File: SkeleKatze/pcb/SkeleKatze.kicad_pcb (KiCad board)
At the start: 2 copper layers, 54.5 x 82.9 mm, 6 parts, among them SW2 SW_Push

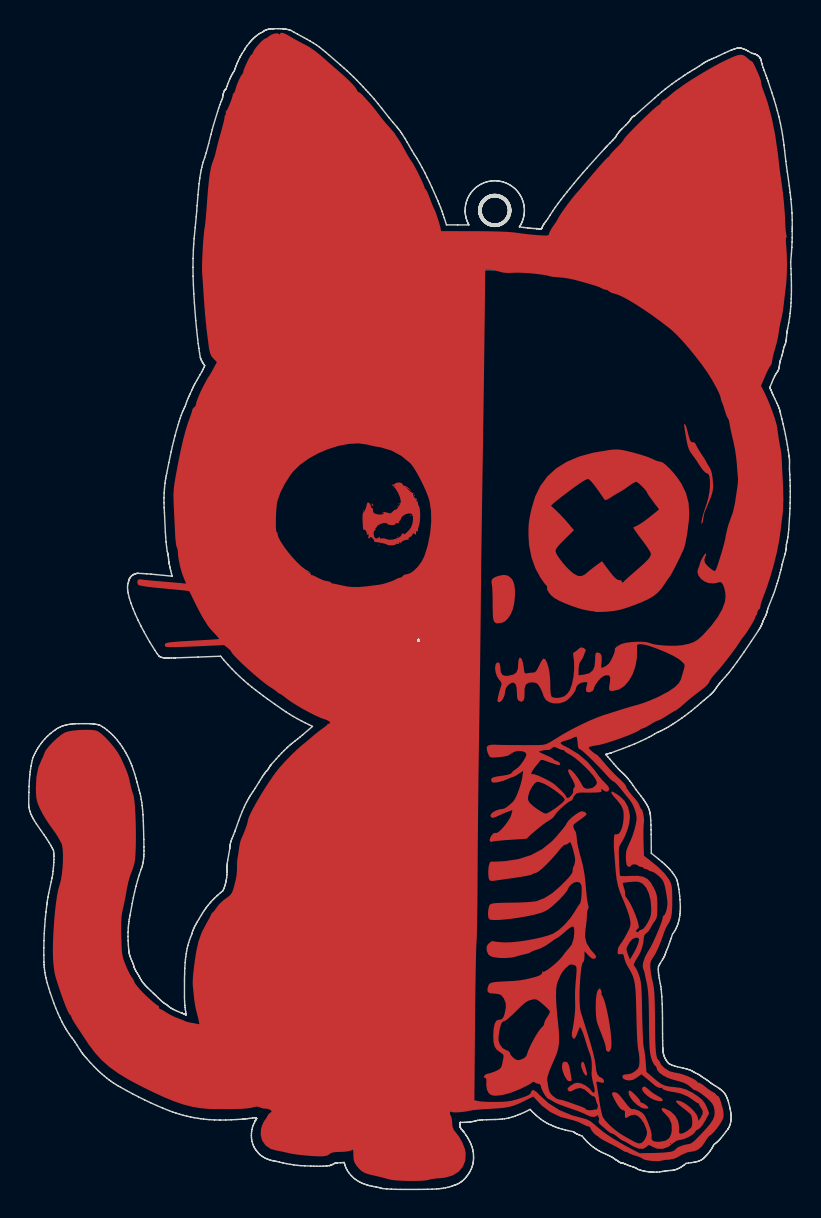
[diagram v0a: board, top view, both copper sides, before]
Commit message: Adds an explicit drill hole rather than relying on an edgecut
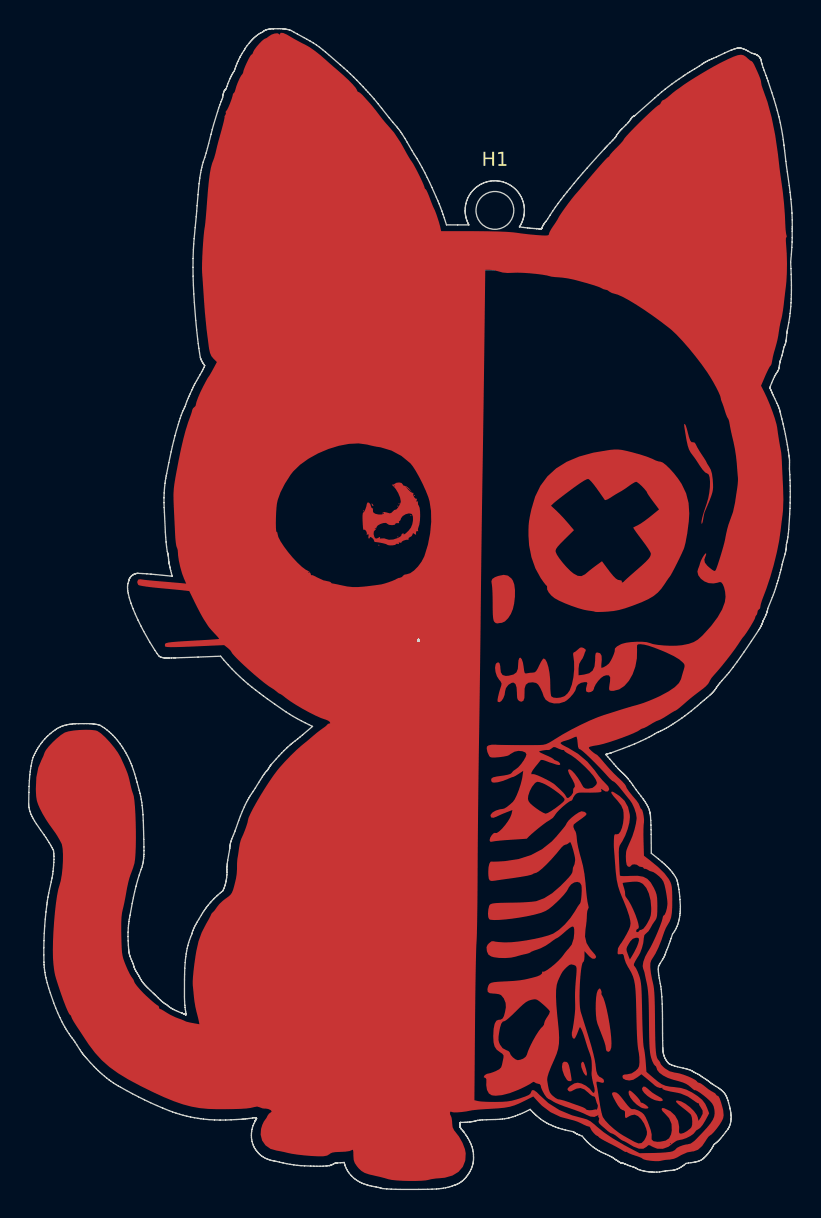
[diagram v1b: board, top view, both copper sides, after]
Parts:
- added H1: MountingHole, MountingHole:MountingHole_2.7mm_M2.5, F.Cu at (221.0, 48.9)
- moved D1 7.18 mm to (203.0, 61.5), turned to -45 degrees
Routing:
- net GND: track 81.6 -> 85.0 mm
- net Net-(D1-A): track 64.0 -> 66.3 mm
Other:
- outline, holes or cut-outs redrawn
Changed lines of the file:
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@@
 		(embedded_fonts no)
 	)
+	(footprint "MountingHole:MountingHole_2.7mm_M2.5"
+		(layer "F.Cu")
+		(at 220.955876 48.864324)
+		(descr "Mounting Hole 2.7mm, M2.5, no annular, generated by kicad-footprint-generator mountinghole.py")
+		(tags "mountinghole M2.5")
+		(property "Reference" "H1"
+			(at 0 -3.65 0)
+			(layer "F.SilkS")
+			(effects
+				(font
+					(size 1 1)
+					(thickness 0.15)
+				)
+			)
+		)
+		(property "Value" "MountingHole"
+			(at 0 3.65 0)
+			(layer "F.Fab")
+			(effects
+				(font
+					(size 1 1)
+					(thickness 0.15)
+				)
+			)
+		)
+		(property "Datasheet" ""
+			(at 0 0 0)
+			(layer "F.Fab")
+			(hide yes)
+			(effects
+				(font
+					(size 1.27 1.27)
+				)
+			)
+		)
+		(property "Description" "Mounting Hole without connection"
+			(at 0 0 0)
+			(layer "F.Fab")
+			(hide yes)
+			(effects
+				(font
+					(size 1.27 1.27)
+				)
+			)
+		)
+		(property ki_fp_filters "MountingHole*")
+		(sheetname "/")
+		(sheetfile "SkeleKatze.kicad_sch")
+		(units
+			(unit
+				(name "A")
+				(pins)
+			)
+		)
+		(duplicate_pad_numbers_are_jumpers no)
+		(fp_circle
+			(center 0 0)
+			(end 2.7 0)
+			(stroke
+				(width 0.15)
+				(type solid)
+			)
+			(fill no)
+			(layer "Cmts.User")
+		)
+		(fp_circle
+			(center 0 0)
+			(end 2.95 0)
+			(stroke
+				(width 0.05)
+				(type solid)
+			)
+			(fill no)
+			(layer "F.CrtYd")
+		)
+		(fp_text user "${REFERENCE}"
+			(at 0 0 0)
+			(layer "F.Fab")
+			(effects
+				(font
+					(size 1 1)
+					(thickness 0.15)
+				)
+			)
+		)
+		(pad "" np_thru_hole circle
+			(at 0 0)
+			(size 2.7 2.7)
+			(drill 2.7)
+			(layers "*.Cu" "*.Mask")
+		)
+		(embedded_fonts no)
+	)
 	(footprint "ZAM-Parts:LED D5.0mm SMD"
 		(layer "B.Cu")
-		(at 209.83 59.300002 -90)
+		(at 203 61.5 -45)
 		(property "Reference" "D1"
-			(at 4.572 -1.27 90)
+			(at 4.572 -1.27 135)
 			(unlocked yes)
 			(layer "B.SilkS")
@@
 		)
 		(property "Value" "LED"
-			(at 0 -4.572 90)
+			(at 0 -4.572 135)
 			(unlocked yes)
 			(layer "B.Fab")
@@
 		)
 		(property "Datasheet" ""
-			(at 0 0 90)
+			(at 0 0 135)
 			(unlocked yes)
 			(layer "B.Fab")
@@
 		)
 		(property "Description" "Light emitting diode"
-			(at 0 0 90)
+			(at 0 0 135)
 			(unlocked yes)
 			(layer "B.Fab")
@@
 		)
 		(property "Sim.Pins" "1=K 2=A"
-			(at 0 0 270)
+			(at 0 0 315)
 			(unlocked yes)
 			(layer "B.Fab")
@@
 		(duplicate_pad_numbers_are_jumpers no)
 		(fp_text user "+"
-			(at -1.016 -5.08 90)
+			(at -1.016 -5.08 135)
 			(unlocked yes)
 			(layer "B.SilkS")
@@
 		)
 		(pad "1" smd roundrect
-			(at 0 0 270)
+			(at 0 0 315)
 			(size 4 1.5)
 			(layers "B.Cu" "B.Mask" "B.Paste")
@@
 		)
 		(pad "2" smd roundrect
-			(at 0 -2.54 270)
+			(at 0 -2.54 315)
 			(size 4 1.5)
 			(layers "B.Cu" "B.Mask" "B.Paste")
@@
 	(gr_poly
 		(pts
-			(xy 221.00091 47.807604) (xy 221.054657 47.811691) (xy 221.107623 47.818422) (xy 221.15974 47.827729)
-			(xy 221.210943 47.839546) (xy 221.261165 47.853808) (xy 221.31034 47.870447) (xy 221.358401 47.889396)
-			(xy 221.405281 47.91059) (xy 221.450914 47.933962) (xy 221.495234 47.959446) (xy 221.538174 47.986974)
-			(xy 221.579667 48.016481) (xy 221.619648 48.047899) (xy 221.658049 48.081163) (xy 221.694804 48.116206)
-			(xy 221.729847 48.152961) (xy 221.763111 48.191362) (xy 221.79453 48.231343) (xy 221.824036 48.272836)
-			(xy 221.851565 48.315776) (xy 221.877048 48.360096) (xy 221.90042 48.405729) (xy 221.921614 48.45261)
-			(xy 221.940564 48.50067) (xy 221.957202 48.549845) (xy 221.971464 48.600067) (xy 221.983281 48.65127)
-			(xy 221.992589 48.703387) (xy 221.999319 48.756352) (xy 222.003406 48.810099) (xy 222.004783 48.864561)
-			(xy 222.003406 48.919022) (xy 221.999319 48.972769) (xy 221.992589 49.025734) (xy 221.983281 49.077851)
-			(xy 221.971464 49.129054) (xy 221.957202 49.179276) (xy 221.940564 49.228451) (xy 221.921614 49.276511)
-			(xy 221.90042 49.323391) (xy 221.877048 49.369025) (xy 221.851565 49.413345) (xy 221.824036 49.456284)
-			(xy 221.79453 49.497778) (xy 221.763111 49.537759) (xy 221.729847 49.57616) (xy 221.694804 49.612915)
-			(xy 221.658049 49.647958) (xy 221.619648 49.681222) (xy 221.579667 49.71264) (xy 221.538174 49.742147)
-			(xy 221.495234 49.769675) (xy 221.450914 49.795159) (xy 221.405281 49.818531) (xy 221.358401 49.839725)
-			(xy 221.31034 49.858675) (xy 221.261165 49.875313) (xy 221.210943 49.889575) (xy 221.15974 49.901392)
-			(xy 221.107623 49.9107) (xy 221.054657 49.91743) (xy 221.00091 49.921517) (xy 220.946449 49.922894)
-			(xy 220.891987 49.921517) (xy 220.83824 49.91743) (xy 220.785274 49.9107) (xy 220.733157 49.901392)
-			(xy 220.681954 49.889575) (xy 220.631732 49.875313) (xy 220.582557 49.858675) (xy 220.534496 49.839725)
-			(xy 220.487616 49.818531) (xy 220.441983 49.795159) (xy 220.397663 49.769675) (xy 220.354723 49.742147)
-			(xy 220.31323 49.71264) (xy 220.273249 49.681222) (xy 220.234848 49.647958) (xy 220.198093 49.612915)
-			(xy 220.16305 49.57616) (xy 220.129786 49.537759) (xy 220.098367 49.497778) (xy 220.068861 49.456284)
-			(xy 220.041332 49.413345) (xy 220.015849 49.369025) (xy 219.992477 49.323391) (xy 219.971283 49.276511)
-			(xy 219.952333 49.228451) (xy 219.935695 49.179276) (xy 219.921433 49.129054) (xy 219.909616 49.077851)
-			(xy 219.900309 49.025734) (xy 219.893578 48.972769) (xy 219.889491 48.919022) (xy 219.888114 48.864561)
-			(xy 219.889491 48.810099) (xy 219.893578 48.756352) (xy 219.900309 48.703387) (xy 219.909616 48.65127)
-			(xy 219.921433 48.600067) (xy 219.935695 48.549845) (xy 219.952333 48.50067) (xy 219.971283 48.45261)
-			(xy 219.992477 48.405729) (xy 220.015849 48.360096) (xy 220.041332 48.315776) (xy 220.068861 48.272836)
-			(xy 220.098367 48.231343) (xy 220.129786 48.191362) (xy 220.16305 48.152961) (xy 220.198093 48.116206)
-			(xy 220.234848 48.081163) (xy 220.273249 48.047899) (xy 220.31323 48.016481) (xy 220.354723 47.986974)
-			(xy 220.397663 47.959446) (xy 220.441983 47.933962) (xy 220.487616 47.91059) (xy 220.534496 47.889396)
-			(xy 220.582557 47.870447) (xy 220.631732 47.853808) (xy 220.681954 47.839546) (xy 220.733157 47.827729)
-			(xy 220.785274 47.818422) (xy 220.83824 47.811691) (xy 220.891987 47.807604) (xy 220.946449 47.806227)
-		)
-		(stroke
-			(width 0.264583)
-			(type solid)
-		)
-		(fill no)
-		(layer "Edge.Cuts")
-	)
-	(gr_poly
-		(pts
 			(xy 205.624234 35.88516) (xy 205.782441 35.891945) (xy 205.86124 35.897955) (xy 205.939707 35.90605)
 			(xy 206.017746 35.916488) (xy 206.09526 35.929524) (xy 206.172153 35.945415) (xy 206.248327 35.964416)
@@
 		)
 		(stroke
-			(width 0.1)
+			(width 0)
 			(type solid)
 		)
@@
 	)
 	(segment
-		(start 209.2 62.6)
-		(end 209.83 61.97)
+		(start 208.74052 52.5)
+		(end 202.702037 58.538483)
 		(width 0.3048)
 		(layer "B.Cu")
@@
 	)
 	(segment
-		(start 214.630002 52.5)
-		(end 209.83 57.300002)
-		(width 0.3048)
-		(layer "B.Cu")
-		(net "GND")
-	)
-	(segment
-		(start 203.6 76.5)
-		(end 203.6 66.8)
-		(width 0.3048)
-		(layer "B.Cu")
-		(net "GND")
-	)
-	(segment
-		(start 209.83 57.300002)
-		(end 209.83 59.300002)
+		(start 209.326 82.226)
+		(end 203 75.9)
 		(width 0.3048)
 		(layer "B.Cu")
@@
 	)
 	(segment
-		(start 209.83 61.97)
-		(end 209.83 59.300002)
+		(start 202.702037 61.202037)
+		(end 203 61.5)
 		(width 0.3048)
 		(layer "B.Cu")
@@
 	(segment
 		(start 228.624527 52.5)
-		(end 214.630002 52.5)
+		(end 208.74052 52.5)
 		(width 0.3048)
 		(layer "B.Cu")
@@
 	)
 	(segment
-		(start 209.326 82.226)
-		(end 203.6 76.5)
+		(start 202.702037 58.538483)
+		(end 202.702037 61.202037)
 		(width 0.3048)
 		(layer "B.Cu")
@@
 	)
 	(segment
-		(start 207.8 62.6)
-		(end 209.2 62.6)
+		(start 203 75.9)
+		(end 203 61.5)
 		(width 0.3048)
 		(layer "B.Cu")
@@
 	)
 	(segment
-		(start 203.6 66.8)
-		(end 207.8 62.6)
+		(start 210.25 53)
+		(end 204.796051 58.453949)
 		(width 0.3048)
 		(layer "B.Cu")
-		(net "GND")
+		(net "Net-(D1-A)")
 	)
 	(segment
-		(start 216.2 53)
-		(end 212.370001 56.829999)
+		(start 236.4 48.1)
+		(end 231.5 53)
 		(width 0.3048)
 		(layer "B.Cu")
@@
 	)
 	(segment
-		(start 207.7 63.5)
-		(end 204.1 67.1)
+		(start 231.5 53)
+		(end 210.25 53)
 		(width 0.3048)
 		(layer "B.Cu")
@@
 	)
 	(segment
-		(start 210.17 63.5)
-		(end 207.7 63.5)
+		(start 204.796051 58.453949)
+		(end 204.796051 59.703949)
 		(width 0.3048)
 		(layer "B.Cu")
@@
 	)
 	(segment
-		(start 212.370001 59.299999)
-		(end 212.370001 61.299999)
+		(start 204.1 67.1)
+		(end 205.094014 66.105986)
 		(width 0.3048)
 		(layer "B.Cu")
@@
 	)
 	(segment
-		(start 212.370001 61.299999)
-		(end 210.17 63.5)
+		(start 205.094014 66.105986)
+		(end 205.094014 60.001912)
 		(width 0.3048)
 		(layer "B.Cu")
@@
 	)
 	(segment
-		(start 236.4 48.1)
-		(end 231.5 53)
+		(start 205.094014 60.001912)
+		(end 204.796051 59.703949)
 		(width 0.3048)
 		(layer "B.Cu")
@@
 	)
 	(segment
-		(start 231.5 53)
-		(end 216.2 53)
-		(width 0.3048)
-		(layer "B.Cu")
-		(net "Net-(D1-A)")
-	)
-	(segment
 		(start 206.822 79.022)
 		(end 214.950999 79.022)
@@
 	)
 	(segment
-		(start 212.370001 56.829999)
-		(end 212.370001 59.299999)
-		(width 0.3048)
-		(layer "B.Cu")
-		(net "Net-(D1-A)")
-	)
-	(segment
 		(start 201.452 108.052)
 		(end 204.4 111)
@@
 		(net "Net-(BT1-+)")
 	)
-	(group ""
-		(members "39551d2a-0ece-4b17-89ed-4c343dc6dc4a" "96b08857-4966-4e4c-a868-49f603ad379f")
-	)
 	(embedded_fonts no)
